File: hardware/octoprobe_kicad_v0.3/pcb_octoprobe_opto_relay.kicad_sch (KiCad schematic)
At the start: 5 parts, among them U701 GAQY221S

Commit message: PCB: Octobus
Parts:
- R1001: renamed from R701; footprint Resistor_SMD:R_0402_1005Metric -> Resistor_SMD:R_0805_2012Metric
- R1002: renamed from R702; value 3k9 -> 390; footprint Resistor_SMD:R_0402_1005Metric -> Resistor_SMD:R_0805_2012Metric
- U1001: renamed from U701; footprint Package_SO:SOP-4_3.8x4.1mm_P2.54mm -> 00_project_library:SOP-4_4.4x4.3mm_P2.54mm
- renumbered D701 to D1001, UR701 to UR1001
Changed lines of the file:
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@@
 		)
 	)
-	(text_box "Calculation of the input resistor\n\nVdiff = 3.3V - Vf = 3.3V- 1.2V = 2.1V\nI_Fon = 0.5mA\nR = 2.1V / 0.5mA = 4.2kOhm\n\nE12: 3.9kOhm"
+	(text_box "Calculation of the input resistor\n\nVdiff = 3.3V - Vf = 3.3V- 1.2V = 2.1V\nI_Fon = 5mA\nR = 2.1V / 5mA = 420 Ohm\n\n390 Ohm"
 		(exclude_from_sim no)
 		(at 31.75 96.52 0)
@@
 		(on_board yes)
 		(dnp no)
-		(property "Reference" "R702"
+		(property "Reference" "R1002"
 			(at 92.71 67.056 90)
 			(effects
@@
 			)
 		)
-		(property "Value" "3k9"
+		(property "Value" "390"
 			(at 92.71 64.6684 90)
 			(effects
@@
 			)
 		)
-		(property "Footprint" "Resistor_SMD:R_0402_1005Metric"
+		(property "Footprint" "Resistor_SMD:R_0805_2012Metric"
 			(at 92.71 66.548 90)
 			(effects
@@
 		(instances
 			(project "pcb_octoprobe"
+				(path "/35c47459-45a7-4753-acae-c8b47e7575e1/6546fe85-dd41-453d-98b0-9b6f35fb87fd/401258f3-4e65-4224-8043-f8fa2b007639"
+					(reference "R1002")
+					(unit 1)
+				)
+				(path "/35c47459-45a7-4753-acae-c8b47e7575e1/6546fe85-dd41-453d-98b0-9b6f35fb87fd/aa228a66-0806-4820-976d-dd91b57f82ce"
+					(reference "R1402")
+					(unit 1)
+				)
 				(path "/35c47459-45a7-4753-acae-c8b47e7575e1/6546fe85-dd41-453d-98b0-9b6f35fb87fd/c4f0e93e-0e5b-4500-9781-4e2df6e7b677"
 					(reference "R702")
@@
 		(on_board yes)
 		(dnp no)
-		(property "Reference" "R701"
+		(property "Reference" "R1001"
 			(at 91.44 51.562 90)
 			(effects
@@
 			)
 		)
-		(property "Footprint" "Resistor_SMD:R_0402_1005Metric"
+		(property "Footprint" "Resistor_SMD:R_0805_2012Metric"
 			(at 91.44 47.752 90)
 			(effects
@@
 		(instances
 			(project "pcb_octoprobe"
+				(path "/35c47459-45a7-4753-acae-c8b47e7575e1/6546fe85-dd41-453d-98b0-9b6f35fb87fd/401258f3-4e65-4224-8043-f8fa2b007639"
+					(reference "R1001")
+					(unit 1)
+				)
+				(path "/35c47459-45a7-4753-acae-c8b47e7575e1/6546fe85-dd41-453d-98b0-9b6f35fb87fd/aa228a66-0806-4820-976d-dd91b57f82ce"
+					(reference "R1401")
+					(unit 1)
+				)
 				(path "/35c47459-45a7-4753-acae-c8b47e7575e1/6546fe85-dd41-453d-98b0-9b6f35fb87fd/c4f0e93e-0e5b-4500-9781-4e2df6e7b677"
 					(reference "R701")
@@
 		(dnp no)
 		(fields_autoplaced yes)
-		(property "Reference" "UR701"
+		(property "Reference" "UR1001"
 			(at 61.595 21.59 0)
 			(effects
@@
 		(instances
 			(project "pcb_octoprobe"
+				(path "/35c47459-45a7-4753-acae-c8b47e7575e1/6546fe85-dd41-453d-98b0-9b6f35fb87fd/401258f3-4e65-4224-8043-f8fa2b007639"
+					(reference "UR1001")
+					(unit 1)
+				)
+				(path "/35c47459-45a7-4753-acae-c8b47e7575e1/6546fe85-dd41-453d-98b0-9b6f35fb87fd/aa228a66-0806-4820-976d-dd91b57f82ce"
+					(reference "UR1401")
+					(unit 1)
+				)
 				(path "/35c47459-45a7-4753-acae-c8b47e7575e1/6546fe85-dd41-453d-98b0-9b6f35fb87fd/c4f0e93e-0e5b-4500-9781-4e2df6e7b677"
 					(reference "UR701")
@@
 		(dnp no)
 		(fields_autoplaced yes)
-		(property "Reference" "D701"
+		(property "Reference" "D1001"
 			(at 101.9175 42.545 0)
 			(effects
@@
 					(size 1.27 1.27)
 				)
+				(hide yes)
 			)
 		)
@@
 		(instances
 			(project "pcb_octoprobe"
+				(path "/35c47459-45a7-4753-acae-c8b47e7575e1/6546fe85-dd41-453d-98b0-9b6f35fb87fd/401258f3-4e65-4224-8043-f8fa2b007639"
+					(reference "D1001")
+					(unit 1)
+				)
+				(path "/35c47459-45a7-4753-acae-c8b47e7575e1/6546fe85-dd41-453d-98b0-9b6f35fb87fd/aa228a66-0806-4820-976d-dd91b57f82ce"
+					(reference "D1401")
+					(unit 1)
+				)
 				(path "/35c47459-45a7-4753-acae-c8b47e7575e1/6546fe85-dd41-453d-98b0-9b6f35fb87fd/c4f0e93e-0e5b-4500-9781-4e2df6e7b677"
 					(reference "D701")
@@
 		(dnp no)
 		(fields_autoplaced yes)
-		(property "Reference" "U701"
+		(property "Reference" "U1001"
 			(at 104.14 58.42 0)
 			(effects
@@
 			)
 		)
-		(property "Footprint" "Package_SO:SOP-4_3.8x4.1mm_P2.54mm"
+		(property "Footprint" "00_project_library:SOP-4_4.4x4.3mm_P2.54mm"
 			(at 99.06 72.39 0)
 			(effects
@@
 		(instances
 			(project "pcb_octoprobe"
+				(path "/35c47459-45a7-4753-acae-c8b47e7575e1/6546fe85-dd41-453d-98b0-9b6f35fb87fd/401258f3-4e65-4224-8043-f8fa2b007639"
+					(reference "U1001")
+					(unit 1)
+				)
+				(path "/35c47459-45a7-4753-acae-c8b47e7575e1/6546fe85-dd41-453d-98b0-9b6f35fb87fd/aa228a66-0806-4820-976d-dd91b57f82ce"
+					(reference "U1401")
+					(unit 1)
+				)
 				(path "/35c47459-45a7-4753-acae-c8b47e7575e1/6546fe85-dd41-453d-98b0-9b6f35fb87fd/c4f0e93e-0e5b-4500-9781-4e2df6e7b677"
 					(reference "U701")
@@
 		(on_board yes)
 		(dnp no)
-		(property "Reference" "#PWR0702"
+		(property "Reference" "#PWR01008"
 			(at 109.22 57.15 0)
 			(effects
@@
 		(instances
 			(project "pcb_octoprobe"
+				(path "/35c47459-45a7-4753-acae-c8b47e7575e1/6546fe85-dd41-453d-98b0-9b6f35fb87fd/401258f3-4e65-4224-8043-f8fa2b007639"
+					(reference "#PWR01008")
+					(unit 1)
+				)
+				(path "/35c47459-45a7-4753-acae-c8b47e7575e1/6546fe85-dd41-453d-98b0-9b6f35fb87fd/aa228a66-0806-4820-976d-dd91b57f82ce"
+					(reference "#PWR01402")
+					(unit 1)
+				)
 				(path "/35c47459-45a7-4753-acae-c8b47e7575e1/6546fe85-dd41-453d-98b0-9b6f35fb87fd/c4f0e93e-0e5b-4500-9781-4e2df6e7b677"
 					(reference "#PWR0702")
@@
 		(on_board yes)
 		(dnp no)
-		(property "Reference" "#PWR0701"
+		(property "Reference" "#PWR01007"
 			(at 93.98 76.2 0)
 			(effects
@@
 		(instances
 			(project "pcb_octoprobe"
+				(path "/35c47459-45a7-4753-acae-c8b47e7575e1/6546fe85-dd41-453d-98b0-9b6f35fb87fd/401258f3-4e65-4224-8043-f8fa2b007639"
+					(reference "#PWR01007")
+					(unit 1)
+				)
+				(path "/35c47459-45a7-4753-acae-c8b47e7575e1/6546fe85-dd41-453d-98b0-9b6f35fb87fd/aa228a66-0806-4820-976d-dd91b57f82ce"
+					(reference "#PWR01401")
+					(unit 1)
+				)
 				(path "/35c47459-45a7-4753-acae-c8b47e7575e1/6546fe85-dd41-453d-98b0-9b6f35fb87fd/c4f0e93e-0e5b-4500-9781-4e2df6e7b677"
 					(reference "#PWR0701")

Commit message: PCB: Oscillator
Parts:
- UR1001: footprint 00_project_library:opctoprobe_relay -> 00_project_library:octoprobe_relay; symbol 00_project_library:opctoprobe_relay -> 00_project_library:octoprobe_relay
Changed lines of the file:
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@@
 	)
 	(symbol
-		(lib_id "00_project_library:opctoprobe_relay")
+		(lib_id "00_project_library:octoprobe_relay")
 		(at 50.8 27.94 0)
 		(unit 1)
@@
 			)
 		)
-		(property "Footprint" "00_project_library:opctoprobe_relay"
+		(property "Footprint" "00_project_library:octoprobe_relay"
 			(at 50.8 27.94 0)
 			(effects

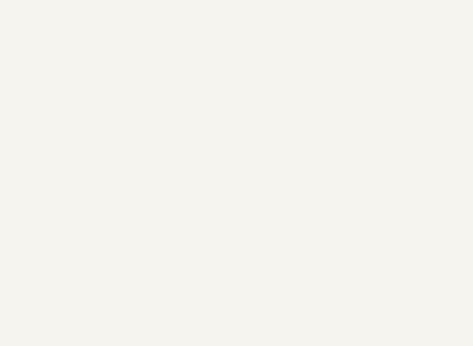
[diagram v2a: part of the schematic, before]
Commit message: PCB: Add "Open Hardware"
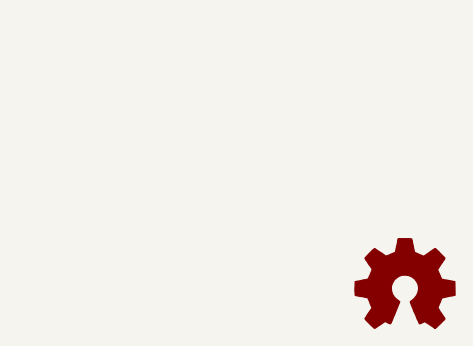
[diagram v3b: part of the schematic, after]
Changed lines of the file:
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@@
+	)
+	(symbol
+		(lib_id "Graphic:Logo_Open_Hardware_Small")
+		(at 274.32 173.99 0)
+		(unit 1)
+		(exclude_from_sim yes)
+		(in_bom no)
+		(on_board no)
+		(dnp no)
+		(fields_autoplaced yes)
+		(property "Reference" "#SYM1101"
+			(at 274.32 167.005 0)
+			(effects
+				(font
+					(size 1.27 1.27)
+				)
+				(hide yes)
+			)
+		)
+		(property "Value" "Logo_Open_Hardware_Small"
+			(at 274.32 179.705 0)
+			(effects
+				(font
+					(size 1.27 1.27)
+				)
+				(hide yes)
+			)
+		)
+		(property "Footprint" ""
+			(at 274.32 173.99 0)
+			(effects
+				(font
+					(size 1.27 1.27)
+				)
+				(hide yes)
+			)
+		)
+		(property "Datasheet" "~"
+			(at 274.32 173.99 0)
+			(effects
+				(font
+					(size 1.27 1.27)
+				)
+				(hide yes)
+			)
+		)
+		(property "Description" "Open Hardware logo, small"
+			(at 274.32 173.99 0)
+			(effects
+				(font
+					(size 1.27 1.27)
+				)
+				(hide yes)
+			)
+		)
+		(instances
+			(project "pcb_octoprobe"
+				(path "/35c47459-45a7-4753-acae-c8b47e7575e1/6546fe85-dd41-453d-98b0-9b6f35fb87fd/401258f3-4e65-4224-8043-f8fa2b007639"
+					(reference "#SYM1101")
+					(unit 1)
+				)
+				(path "/35c47459-45a7-4753-acae-c8b47e7575e1/6546fe85-dd41-453d-98b0-9b6f35fb87fd/aa228a66-0806-4820-976d-dd91b57f82ce"
+					(reference "#SYM1201")
+					(unit 1)
+				)
+				(path "/35c47459-45a7-4753-acae-c8b47e7575e1/6546fe85-dd41-453d-98b0-9b6f35fb87fd/c4f0e93e-0e5b-4500-9781-4e2df6e7b677"
+					(reference "#SYM1001")
+					(unit 1)
+				)
+				(path "/35c47459-45a7-4753-acae-c8b47e7575e1/6546fe85-dd41-453d-98b0-9b6f35fb87fd/e7ee32a2-f587-4a93-9710-ec8609dfb50b"
+					(reference "#SYM701")
+					(unit 1)
+				)
+				(path "/35c47459-45a7-4753-acae-c8b47e7575e1/6546fe85-dd41-453d-98b0-9b6f35fb87fd/ef104267-4346-4f2e-9eff-a3788359729c"
+					(reference "#SYM601")
+					(unit 1)
+				)
+				(path "/35c47459-45a7-4753-acae-c8b47e7575e1/6546fe85-dd41-453d-98b0-9b6f35fb87fd/f26e04d3-5a13-44f7-8e87-f1ee92fb659b"
+					(reference "#SYM801")
+					(unit 1)
+				)
+				(path "/35c47459-45a7-4753-acae-c8b47e7575e1/6546fe85-dd41-453d-98b0-9b6f35fb87fd/fdcd82e4-82d2-49d0-afb5-eac182e2d36c"
+					(reference "#SYM901")
+					(unit 1)
+				)
+			)
+		)
 	)
 	(symbol

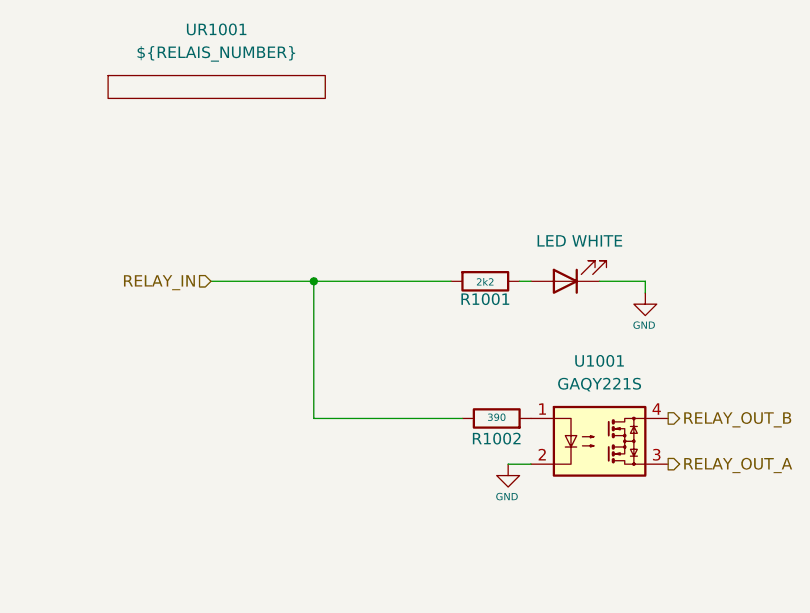
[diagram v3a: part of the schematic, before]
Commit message: PCB: Production files ready
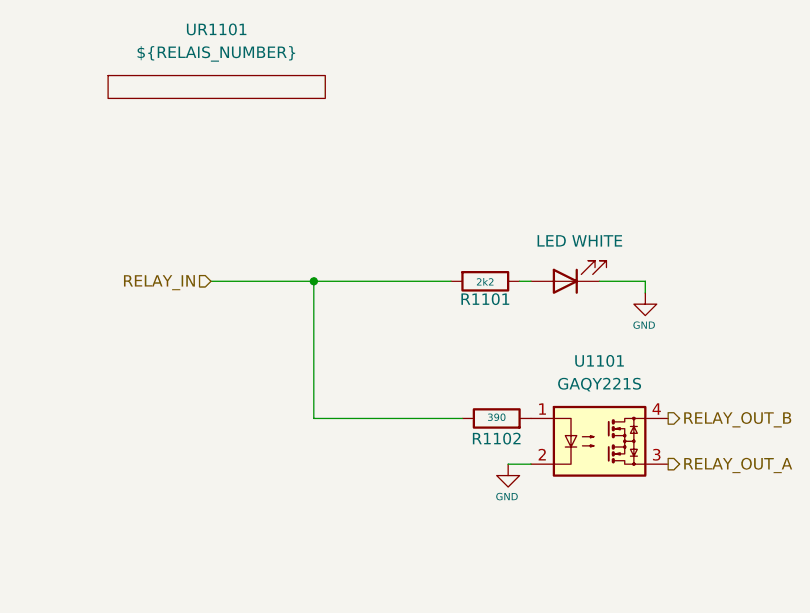
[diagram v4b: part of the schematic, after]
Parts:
- renumbered D1001 to D1101, R1001 to R1101, R1002 to R1102, U1001 to U1101, UR1001 to UR1101
